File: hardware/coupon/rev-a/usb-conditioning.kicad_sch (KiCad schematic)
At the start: 30 parts, among them U24 SN74LVC2G17DBVR, U25 SN74LVC2G17DBVR, U26 SN74LVC2G17DBVR, U27 SN74LVC2G17DBVR, U28 SN74LVC2G17DBVR

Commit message: Capture USB detection and switched data path after native logic review
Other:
- note added: "+3V3_USB is supplied by U29 on usb-interface; its protected 5 V input is still a draft boundary."
- note added: "CHG_DET uses the staged 4.80-5.25 V USB supply boundary; protection is pending. ESP_RUNNING is not tied to ESP_EN."
- note added: "OUT1/OUT2 and BC outputs come from usb-interface. Supervisors, switch and MCU inputs remain test boundaries."
- note added: "USB input conditioning: detector outputs connected; five supervisor/application inputs remain staged"
- note removed: "CHG_DET may be VBUS-level only after input protection bounds it to 5.5 V. ESP_RUNNING is not yet tied to ESP_EN."
- note removed: "Draft +3V3_USB source assumption; remove/replace when the actual USB LDO is captured."
- note removed: "No detector, supervisor, switch or MCU request is connected here yet. Pull defaults implement the inactive contract only."
- note removed: "USB input conditioning: five dual Schmitt buffers; all ten source signals remain test boundaries"
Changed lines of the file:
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@@
 (kicad_sch (version 20260306) (generator "rgb_badge_permission") (generator_version "1.0")
  (paper "A2")
-(title_block (title "Coupon Rev A - USB input conditioning (staged)") (rev "A-draft") (comment 1 "SPDX-License-Identifier: CERN-OHL-S-2.0") (comment 2 "Staged logic capture; detector/supervisor and charger actuator boundaries are NOT closed"))
-(text "USB input conditioning: five dual Schmitt buffers; all ten source signals remain test boundaries" (at 20.320 20.320 0) (effects (font (size 2 2)) (justify left)))
-(text "No detector, supervisor, switch or MCU request is connected here yet. Pull defaults implement the inactive contract only." (at 20.320 30.480 0) (effects (font (size 1.27 1.27)) (justify left)))
-(text "CHG_DET may be VBUS-level only after input protection bounds it to 5.5 V. ESP_RUNNING is not yet tied to ESP_EN." (at 20.320 38.100 0) (effects (font (size 1.27 1.27)) (justify left)))
+(title_block (title "Coupon Rev A - USB input conditioning (staged)") (rev "A-draft") (comment 1 "SPDX-License-Identifier: CERN-OHL-S-2.0") (comment 2 "Staged logic; supervisors, startup inhibit and charger actuation remain open"))
+(text "USB input conditioning: detector outputs connected; five supervisor/application inputs remain staged" (at 20.320 20.320 0) (effects (font (size 2 2)) (justify left)))
+(text "OUT1/OUT2 and BC outputs come from usb-interface. Supervisors, switch and MCU inputs remain test boundaries." (at 20.320 30.480 0) (effects (font (size 1.27 1.27)) (justify left)))
+(text "CHG_DET uses the staged 4.80-5.25 V USB supply boundary; protection is pending. ESP_RUNNING is not tied to ESP_EN." (at 20.320 38.100 0) (effects (font (size 1.27 1.27)) (justify left)))
 (text "OUT1 / OUT2: conditioned before ordinary LVC gates" (at 22.860 55.880 0) (effects (font (size 1.016 1.016)) (justify left)))
 (symbol (lib_id "rgb-badge-coupon:SN74LVC2G17DBVR") (at 83.820 76.200 0) (unit 1)
@@
 (wire (pts (xy 505.460 350.520) (xy 495.300 350.520)) (stroke (width 0) (type default)))
 (global_label "USB_RAW_USB_REQUEST" (shape passive) (at 495.300 350.520 180) (effects (font (size 1.016 1.016)) (justify right)) (property "Intersheetrefs" "${INTERSHEET_REFS}" (at 495.300 350.520 0) (effects (font (size 1.27 1.27)) (hide yes))))
-(symbol (lib_id "rgb-badge-coupon:PWR_FLAG") (at 444.500 218.440 0) (unit 1)
-(exclude_from_sim no) (in_bom no) (on_board no) (dnp no)
-(property "Reference" "#FLG04" (at 444.500 212.090 0) (effects (font (size 1.27 1.27)) (hide yes)))
-(property "Value" "PWR_FLAG" (at 444.500 214.630 0) (effects (font (size 1.27 1.27))))
-(property "Footprint" "" (at 444.500 218.440 0) (effects (font (size 1.27 1.27)) (hide yes)))
-(property "Datasheet" "" (at 444.500 218.440 0) (effects (font (size 1.27 1.27)) (hide yes)))
-(property "Manufacturer" "" (at 444.500 218.440 0) (effects (font (size 1.27 1.27)) (hide yes)))
-(property "MPN" "" (at 444.500 218.440 0) (effects (font (size 1.27 1.27)) (hide yes)))
-(pin "1")
-(instances (project "rgb-badge-coupon" (path "/207fb68e-2ddb-46bb-8712-eba2f8c5eef6/05e96674-5624-545e-aef0-a1af37c3f4ba" (reference "#FLG04") (unit 1)))))
-(wire (pts (xy 444.500 218.440) (xy 454.660 218.440)) (stroke (width 0) (type default)))
-(global_label "+3V3_USB" (shape passive) (at 454.660 218.440 0) (effects (font (size 1.016 1.016)) (justify left)) (property "Intersheetrefs" "${INTERSHEET_REFS}" (at 454.660 218.440 0) (effects (font (size 1.27 1.27)) (hide yes))))
-(text "Draft +3V3_USB source assumption; remove/replace when the actual USB LDO is captured." (at 378.460 241.300 0) (effects (font (size 1.016 1.016)) (justify left)))
+(text "+3V3_USB is supplied by U29 on usb-interface; its protected 5 V input is still a draft boundary." (at 378.460 241.300 0) (effects (font (size 1.016 1.016)) (justify left)))
 (text "Default pull-ups: 10 kohm. Default pull-downs: 100 kohm. Source/leakage/suspend budgets remain to be qualified." (at 20.320 375.920 0) (effects (font (size 1.27 1.27)) (justify left)))
 (embedded_fonts no)

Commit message: Review native USB capture and add staged logic-rail supervision
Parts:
- added C38: 100n 16V X7R, rgb-badge-coupon:C_Murata_GRM15_0402, symbol rgb-badge-coupon:GRM155R71C104KA88D
- added R75: 620k 1%, rgb-badge-coupon:R_Panasonic_ERJ2_0402, symbol rgb-badge-coupon:ERJ-2RKF6203X
- added R76, R77: 100k 1%, rgb-badge-coupon:R_Panasonic_ERJ2_0402, symbol rgb-badge-coupon:ERJ-2RKF1003X
- added R78: 10k 1%, rgb-badge-coupon:R_Panasonic_ERJ2_0402, symbol rgb-badge-coupon:ERJ-2RKF1002X
- added U34: TPS3808G01DBVR, rgb-badge-coupon:SOT23_TI_DBV0006A, symbol rgb-badge-coupon:TPS3808G01DBVR
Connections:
- net +3V3_USB: now also R75.1, R78.1
- net GND: now also C38.2, R76.2, U34.2 (GND)
- net USB_RAW_LOGIC_READY: now also R78.2, U34.1 (RESET)
- new net +5V_USB: C38.1, R77.1, U34.3 (MR), U34.6 (VDD)
- new net USB_LOGIC_CT: R77.2, U34.4 (CT)
- new net USB_LOGIC_SENSE: R75.2, R76.1, U34.5 (SENSE)
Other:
- note added: "Logic-rail supervisor: input-domain powered, delayed release"
- note added: "OUT1/OUT2 and BC outputs come from usb-interface. VBUS_VALID, switch and MCU inputs remain test boundaries."
- note added: "U34: nominal trip 2.916 V; CT via 100k selects 180-420 ms release. Fast brownout/actuator inhibition remain unproven."
- note added: "USB input conditioning: detectors and logic-rail supervisor connected; four inputs remain staged"
- note removed: "+3V3_USB is supplied by U29 on usb-interface; its protected 5 V input is still a draft boundary."
- note removed: "OUT1/OUT2 and BC outputs come from usb-interface. Supervisors, switch and MCU inputs remain test boundaries."
- note removed: "USB input conditioning: detector outputs connected; five supervisor/application inputs remain staged"

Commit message: Simplify charging to Type-C-only fixed-current policy
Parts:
- removed C26, C27, C28: 100n 16V X7R, rgb-badge-coupon:C_Murata_GRM15_0402, symbol rgb-badge-coupon:GRM155R71C104KA88D
- removed R64: 10k 1%, rgb-badge-coupon:R_Panasonic_ERJ2_0402, symbol rgb-badge-coupon:ERJ-2RKF1002X
- removed R65, R66, R67, R68, R69: 100k 1%, rgb-badge-coupon:R_Panasonic_ERJ2_0402, symbol rgb-badge-coupon:ERJ-2RKF1003X
- removed TP24: SW_OPEN, rgb-badge-coupon:TestPoint_Pad_D1.0mm, symbol rgb-badge-coupon:TestPoint_Pad
- removed TP25: VBUS_VALID, rgb-badge-coupon:TestPoint_Pad_D1.0mm, symbol rgb-badge-coupon:TestPoint_Pad
- removed TP26: LOGIC_READY, rgb-badge-coupon:TestPoint_Pad_D1.0mm, symbol rgb-badge-coupon:TestPoint_Pad
- removed TP27: SWITCH_ON, rgb-badge-coupon:TestPoint_Pad_D1.0mm, symbol rgb-badge-coupon:TestPoint_Pad
- removed TP28: ESP_RUNNING, rgb-badge-coupon:TestPoint_Pad_D1.0mm, symbol rgb-badge-coupon:TestPoint_Pad
- removed TP29: USB_REQUEST, rgb-badge-coupon:TestPoint_Pad_D1.0mm, symbol rgb-badge-coupon:TestPoint_Pad
- removed U26, U27, U28: SN74LVC2G17DBVR, rgb-badge-coupon:SOT23_TI_DBV0006A, symbol rgb-badge-coupon:SN74LVC2G17DBVR
- R62: value 10k 1% -> 100k 1%; symbol rgb-badge-coupon:ERJ-2RKF1002X -> rgb-badge-coupon:ERJ-2RKF1003X; MPN ERJ-2RKF1002X -> ERJ-2RKF1003X
- TP22: value CHG_AL_N -> VBUS_VALID
- TP23: value CHG_DET -> LOGIC_READY
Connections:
- net USB_CHG_AL_N is gone; now on net USB_VBUS_VALID: U25.6 (1Y)
- net USB_CHG_DET is gone; now on net USB_LOGIC_READY: U25.4 (2Y)
- net USB_RAW_CHG_AL_N is gone; now on net USB_RAW_VBUS_VALID: R62.1, TP22.1, U25.1 (1A)
- net USB_RAW_CHG_DET is gone; now on net USB_RAW_LOGIC_READY: R63.1, TP23.1, U25.3 (2A)
- net +3V3_USB: no longer R62.2
- net GND: now also R62.2
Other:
- note added: "ADR 0013: Type-C detector and logic supervisor; VBUS qualification remains staged"
- note added: "No BC1.2 or application-domain inputs. Default-current and USB-A sources cannot grant charging."
- note added: "OUT1/OUT2 come from usb-interface. Only VBUS_VALID remains an external qualification boundary."
- note added: "VBUS_VALID / LOGIC_READY: conditioned before ordinary LVC gates"
- note removed: "CHG_AL_N / CHG_DET: conditioned before ordinary LVC gates"
- note removed: "CHG_DET uses the staged 4.80-5.25 V USB supply boundary; protection is pending. ESP_RUNNING is not tied to ESP_EN."
- note removed: "ESP_RUNNING / USB_REQUEST: conditioned before ordinary LVC gates"
- note removed: "LOGIC_READY / SWITCH_ON: conditioned before ordinary LVC gates"
- note removed: "OUT1/OUT2 and BC outputs come from usb-interface. VBUS_VALID, switch and MCU inputs remain test boundaries."
- note removed: "SW_OPEN / VBUS_VALID: conditioned before ordinary LVC gates"
- note removed: "USB input conditioning: detectors and logic-rail supervisor connected; four inputs remain staged"

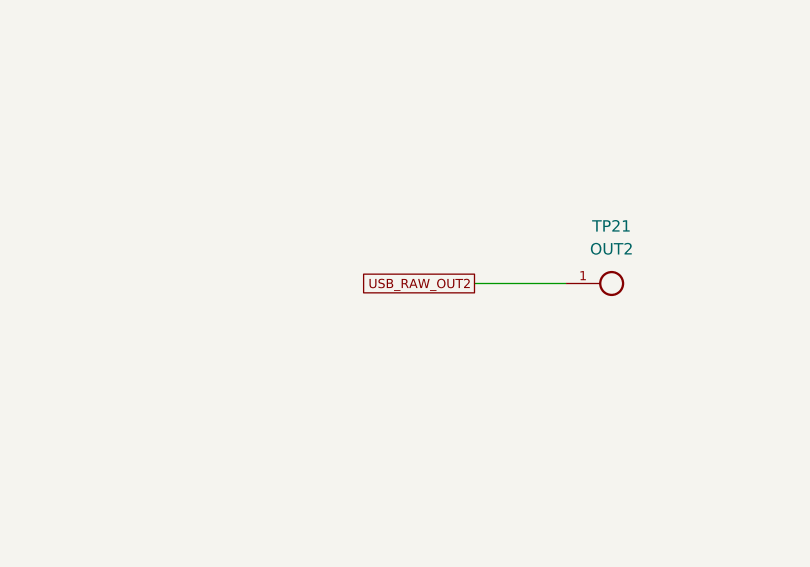
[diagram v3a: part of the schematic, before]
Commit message: Terminate conditioned OUT2 on its diagnostic test pad
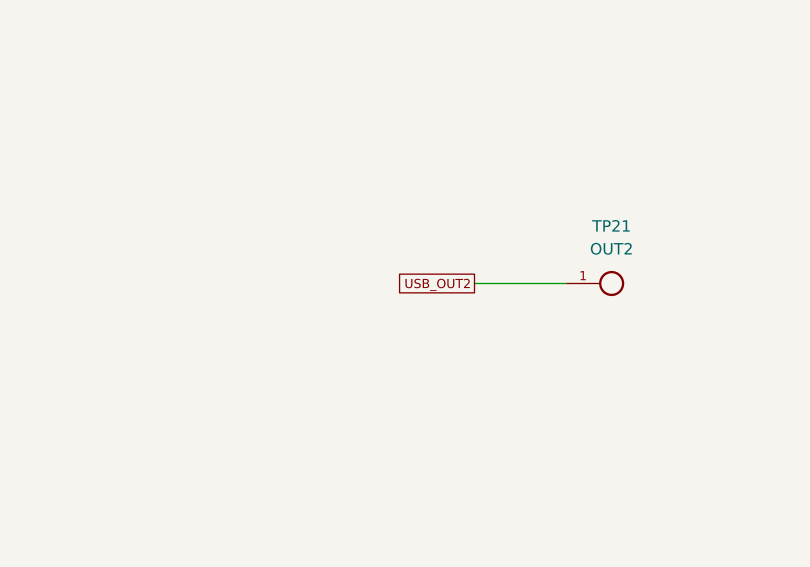
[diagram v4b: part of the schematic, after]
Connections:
- net USB_OUT2: now also TP21.1
- net USB_RAW_OUT2: no longer TP21.1
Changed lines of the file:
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@@
 (instances (project "rgb-badge-coupon" (path "/207fb68e-2ddb-46bb-8712-eba2f8c5eef6/05e96674-5624-545e-aef0-a1af37c3f4ba" (reference "TP21") (unit 1)))))
 (wire (pts (xy 185.420 325.120) (xy 175.260 325.120)) (stroke (width 0) (type default)))
-(global_label "USB_RAW_OUT2" (shape passive) (at 175.260 325.120 180) (effects (font (size 1.016 1.016)) (justify right)) (property "Intersheetrefs" "${INTERSHEET_REFS}" (at 175.260 325.120 0) (effects (font (size 1.27 1.27)) (hide yes))))
+(global_label "USB_OUT2" (shape passive) (at 175.260 325.120 180) (effects (font (size 1.016 1.016)) (justify right)) (property "Intersheetrefs" "${INTERSHEET_REFS}" (at 175.260 325.120 0) (effects (font (size 1.27 1.27)) (hide yes))))
 (symbol (lib_id "rgb-badge-coupon:TestPoint_Pad") (at 297.180 325.120 0) (unit 1)
 (exclude_from_sim no) (in_bom no) (on_board yes) (dnp no)

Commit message: Normalize Panasonic ERJ order codes across coupon
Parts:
- R60, R61, R78: symbol rgb-badge-coupon:ERJ-2RKF1002X -> rgb-badge-coupon:ERJ2RKF1002X; MPN ERJ-2RKF1002X -> ERJ2RKF1002X
- R62, R63, R76, R77: symbol rgb-badge-coupon:ERJ-2RKF1003X -> rgb-badge-coupon:ERJ2RKF1003X; MPN ERJ-2RKF1003X -> ERJ2RKF1003X
- R75: symbol rgb-badge-coupon:ERJ-2RKF6203X -> rgb-badge-coupon:ERJ2RKF6203X; MPN ERJ-2RKF6203X -> ERJ2RKF6203X
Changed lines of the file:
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@@
 (wire (pts (xy 88.900 99.060) (xy 99.060 99.060)) (stroke (width 0) (type default)))
 (global_label "GND" (shape passive) (at 99.060 99.060 0) (effects (font (size 1.016 1.016)) (justify left)) (property "Intersheetrefs" "${INTERSHEET_REFS}" (at 99.060 99.060 0) (effects (font (size 1.27 1.27)) (hide yes))))
-(symbol (lib_id "rgb-badge-coupon:ERJ-2RKF1002X") (at 83.820 121.920 0) (unit 1)
+(symbol (lib_id "rgb-badge-coupon:ERJ2RKF1002X") (at 83.820 121.920 0) (unit 1)
 (exclude_from_sim no) (in_bom yes) (on_board yes) (dnp no)
 (property "Reference" "R60" (at 83.820 115.570 0) (effects (font (size 1.27 1.27))))
@@
 (property "Datasheet" "https://industrial.panasonic.com/cdbs/www-data/pdf/RDA0000/AOA0000C304.pdf" (at 83.820 121.920 0) (effects (font (size 1.27 1.27)) (hide yes)))
 (property "Manufacturer" "Panasonic" (at 83.820 121.920 0) (effects (font (size 1.27 1.27)) (hide yes)))
-(property "MPN" "ERJ-2RKF1002X" (at 83.820 121.920 0) (effects (font (size 1.27 1.27)) (hide yes)))
+(property "MPN" "ERJ2RKF1002X" (at 83.820 121.920 0) (effects (font (size 1.27 1.27)) (hide yes)))
 (pin "1")
 (pin "2")
@@
 (wire (pts (xy 88.900 121.920) (xy 99.060 121.920)) (stroke (width 0) (type default)))
 (global_label "+3V3_USB" (shape passive) (at 99.060 121.920 0) (effects (font (size 1.016 1.016)) (justify left)) (property "Intersheetrefs" "${INTERSHEET_REFS}" (at 99.060 121.920 0) (effects (font (size 1.27 1.27)) (hide yes))))
-(symbol (lib_id "rgb-badge-coupon:ERJ-2RKF1002X") (at 83.820 142.240 0) (unit 1)
+(symbol (lib_id "rgb-badge-coupon:ERJ2RKF1002X") (at 83.820 142.240 0) (unit 1)
 (exclude_from_sim no) (in_bom yes) (on_board yes) (dnp no)
 (property "Reference" "R61" (at 83.820 135.890 0) (effects (font (size 1.27 1.27))))
@@
 (property "Datasheet" "https://industrial.panasonic.com/cdbs/www-data/pdf/RDA0000/AOA0000C304.pdf" (at 83.820 142.240 0) (effects (font (size 1.27 1.27)) (hide yes)))
 (property "Manufacturer" "Panasonic" (at 83.820 142.240 0) (effects (font (size 1.27 1.27)) (hide yes)))
-(property "MPN" "ERJ-2RKF1002X" (at 83.820 142.240 0) (effects (font (size 1.27 1.27)) (hide yes)))
+(property "MPN" "ERJ2RKF1002X" (at 83.820 142.240 0) (effects (font (size 1.27 1.27)) (hide yes)))
 (pin "1")
 (pin "2")
@@
 (wire (pts (xy 269.240 99.060) (xy 279.400 99.060)) (stroke (width 0) (type default)))
 (global_label "GND" (shape passive) (at 279.400 99.060 0) (effects (font (size 1.016 1.016)) (justify left)) (property "Intersheetrefs" "${INTERSHEET_REFS}" (at 279.400 99.060 0) (effects (font (size 1.27 1.27)) (hide yes))))
-(symbol (lib_id "rgb-badge-coupon:ERJ-2RKF1003X") (at 264.160 121.920 0) (unit 1)
+(symbol (lib_id "rgb-badge-coupon:ERJ2RKF1003X") (at 264.160 121.920 0) (unit 1)
 (exclude_from_sim no) (in_bom yes) (on_board yes) (dnp no)
 (property "Reference" "R62" (at 264.160 115.570 0) (effects (font (size 1.27 1.27))))
@@
 (property "Datasheet" "https://industrial.panasonic.com/cdbs/www-data/pdf/RDA0000/AOA0000C304.pdf" (at 264.160 121.920 0) (effects (font (size 1.27 1.27)) (hide yes)))
 (property "Manufacturer" "Panasonic" (at 264.160 121.920 0) (effects (font (size 1.27 1.27)) (hide yes)))
-(property "MPN" "ERJ-2RKF1003X" (at 264.160 121.920 0) (effects (font (size 1.27 1.27)) (hide yes)))
+(property "MPN" "ERJ2RKF1003X" (at 264.160 121.920 0) (effects (font (size 1.27 1.27)) (hide yes)))
 (pin "1")
 (pin "2")
@@
 (wire (pts (xy 269.240 121.920) (xy 279.400 121.920)) (stroke (width 0) (type default)))
 (global_label "GND" (shape passive) (at 279.400 121.920 0) (effects (font (size 1.016 1.016)) (justify left)) (property "Intersheetrefs" "${INTERSHEET_REFS}" (at 279.400 121.920 0) (effects (font (size 1.27 1.27)) (hide yes))))
-(symbol (lib_id "rgb-badge-coupon:ERJ-2RKF1003X") (at 264.160 142.240 0) (unit 1)
+(symbol (lib_id "rgb-badge-coupon:ERJ2RKF1003X") (at 264.160 142.240 0) (unit 1)
 (exclude_from_sim no) (in_bom yes) (on_board yes) (dnp no)
 (property "Reference" "R63" (at 264.160 135.890 0) (effects (font (size 1.27 1.27))))
@@
 (property "Datasheet" "https://industrial.panasonic.com/cdbs/www-data/pdf/RDA0000/AOA0000C304.pdf" (at 264.160 142.240 0) (effects (font (size 1.27 1.27)) (hide yes)))
 (property "Manufacturer" "Panasonic" (at 264.160 142.240 0) (effects (font (size 1.27 1.27)) (hide yes)))
-(property "MPN" "ERJ-2RKF1003X" (at 264.160 142.240 0) (effects (font (size 1.27 1.27)) (hide yes)))
+(property "MPN" "ERJ2RKF1003X" (at 264.160 142.240 0) (effects (font (size 1.27 1.27)) (hide yes)))
 (pin "1")
 (pin "2")
@@
 (wire (pts (xy 449.580 218.440) (xy 459.740 218.440)) (stroke (width 0) (type default)))
 (global_label "GND" (shape passive) (at 459.740 218.440 0) (effects (font (size 1.016 1.016)) (justify left)) (property "Intersheetrefs" "${INTERSHEET_REFS}" (at 459.740 218.440 0) (effects (font (size 1.27 1.27)) (hide yes))))
-(symbol (lib_id "rgb-badge-coupon:ERJ-2RKF6203X") (at 444.500 238.760 0) (unit 1)
+(symbol (lib_id "rgb-badge-coupon:ERJ2RKF6203X") (at 444.500 238.760 0) (unit 1)
 (exclude_from_sim no) (in_bom yes) (on_board yes) (dnp no)
 (property "Reference" "R75" (at 444.500 232.410 0) (effects (font (size 1.27 1.27))))
@@
 (property "Datasheet" "https://industrial.panasonic.com/cdbs/www-data/pdf/RDA0000/AOA0000C304.pdf" (at 444.500 238.760 0) (effects (font (size 1.27 1.27)) (hide yes)))
 (property "Manufacturer" "Panasonic" (at 444.500 238.760 0) (effects (font (size 1.27 1.27)) (hide yes)))
-(property "MPN" "ERJ-2RKF6203X" (at 444.500 238.760 0) (effects (font (size 1.27 1.27)) (hide yes)))
+(property "MPN" "ERJ2RKF6203X" (at 444.500 238.760 0) (effects (font (size 1.27 1.27)) (hide yes)))
 (pin "1")
 (pin "2")
@@
 (wire (pts (xy 449.580 238.760) (xy 459.740 238.760)) (stroke (width 0) (type default)))
 (global_label "USB_LOGIC_SENSE" (shape passive) (at 459.740 238.760 0) (effects (font (size 1.016 1.016)) (justify left)) (property "Intersheetrefs" "${INTERSHEET_REFS}" (at 459.740 238.760 0) (effects (font (size 1.27 1.27)) (hide yes))))
-(symbol (lib_id "rgb-badge-coupon:ERJ-2RKF1003X") (at 444.500 259.080 0) (unit 1)
+(symbol (lib_id "rgb-badge-coupon:ERJ2RKF1003X") (at 444.500 259.080 0) (unit 1)
 (exclude_from_sim no) (in_bom yes) (on_board yes) (dnp no)
 (property "Reference" "R76" (at 444.500 252.730 0) (effects (font (size 1.27 1.27))))
@@
 (property "Datasheet" "https://industrial.panasonic.com/cdbs/www-data/pdf/RDA0000/AOA0000C304.pdf" (at 444.500 259.080 0) (effects (font (size 1.27 1.27)) (hide yes)))
 (property "Manufacturer" "Panasonic" (at 444.500 259.080 0) (effects (font (size 1.27 1.27)) (hide yes)))
-(property "MPN" "ERJ-2RKF1003X" (at 444.500 259.080 0) (effects (font (size 1.27 1.27)) (hide yes)))
+(property "MPN" "ERJ2RKF1003X" (at 444.500 259.080 0) (effects (font (size 1.27 1.27)) (hide yes)))
 (pin "1")
 (pin "2")
@@
 (wire (pts (xy 449.580 259.080) (xy 459.740 259.080)) (stroke (width 0) (type default)))
 (global_label "GND" (shape passive) (at 459.740 259.080 0) (effects (font (size 1.016 1.016)) (justify left)) (property "Intersheetrefs" "${INTERSHEET_REFS}" (at 459.740 259.080 0) (effects (font (size 1.27 1.27)) (hide yes))))
-(symbol (lib_id "rgb-badge-coupon:ERJ-2RKF1003X") (at 444.500 279.400 0) (unit 1)
+(symbol (lib_id "rgb-badge-coupon:ERJ2RKF1003X") (at 444.500 279.400 0) (unit 1)
 (exclude_from_sim no) (in_bom yes) (on_board yes) (dnp no)
 (property "Reference" "R77" (at 444.500 273.050 0) (effects (font (size 1.27 1.27))))
@@
 (property "Datasheet" "https://industrial.panasonic.com/cdbs/www-data/pdf/RDA0000/AOA0000C304.pdf" (at 444.500 279.400 0) (effects (font (size 1.27 1.27)) (hide yes)))
 (property "Manufacturer" "Panasonic" (at 444.500 279.400 0) (effects (font (size 1.27 1.27)) (hide yes)))
-(property "MPN" "ERJ-2RKF1003X" (at 444.500 279.400 0) (effects (font (size 1.27 1.27)) (hide yes)))
+(property "MPN" "ERJ2RKF1003X" (at 444.500 279.400 0) (effects (font (size 1.27 1.27)) (hide yes)))
 (pin "1")
 (pin "2")
@@
 (wire (pts (xy 449.580 279.400) (xy 459.740 279.400)) (stroke (width 0) (type default)))
 (global_label "USB_LOGIC_CT" (shape passive) (at 459.740 279.400 0) (effects (font (size 1.016 1.016)) (justify left)) (property "Intersheetrefs" "${INTERSHEET_REFS}" (at 459.740 279.400 0) (effects (font (size 1.27 1.27)) (hide yes))))
-(symbol (lib_id "rgb-badge-coupon:ERJ-2RKF1002X") (at 444.500 299.720 0) (unit 1)
+(symbol (lib_id "rgb-badge-coupon:ERJ2RKF1002X") (at 444.500 299.720 0) (unit 1)
 (exclude_from_sim no) (in_bom yes) (on_board yes) (dnp no)
 (property "Reference" "R78" (at 444.500 293.370 0) (effects (font (size 1.27 1.27))))
@@
 (property "Datasheet" "https://industrial.panasonic.com/cdbs/www-data/pdf/RDA0000/AOA0000C304.pdf" (at 444.500 299.720 0) (effects (font (size 1.27 1.27)) (hide yes)))
 (property "Manufacturer" "Panasonic" (at 444.500 299.720 0) (effects (font (size 1.27 1.27)) (hide yes)))
-(property "MPN" "ERJ-2RKF1002X" (at 444.500 299.720 0) (effects (font (size 1.27 1.27)) (hide yes)))
-(pin "1")
-(pin "2")
+(property "MPN" "ERJ2RKF1002X" (at 444.500 299.720 0) (effects (font (size 1.27 1.27)) (hide yes)))
+(pin "1")
+(pin "2")
